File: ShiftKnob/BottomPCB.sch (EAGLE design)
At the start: 36 parts, among them IC2 UA78M05DCY, J1 AVR_SPI_PRG_6PTH, Q1 16MHz, Q2 MOSFET-NCHANNELSMD, Q3 MOSFET-PCHANNELSMD, Q4 MOSFET-NCHANNELSMD, Q5 MOSFET-NCHANNELSMD, Q6 MOSFET-NCHANNELSMD, U1 ATMEGA328, U3 FT232RL-BASICSSOP

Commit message: add 0.1" holes in bottom PCB.
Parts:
- added JP2, JP5: (no value), SparkFun-Connectors:M03PTH
- added U$2: 7-SEGMENT-DISPLAY-1"-RED, SparkFun-Displays:7-SEGMENT-DISPLAY-1"-RED
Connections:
- new net N$20: JP2.2
- new net N$26: JP2.1
- new net N$27: JP5.3
- new net N$28: JP5.2
- new net N$29: JP5.1
- new net N$3: JP2.3
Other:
- moved on the sheet: JP1
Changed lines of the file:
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@@
 <setting verticaltext="up"/>
 </settings>
-<grid distance="0.05" unitdist="inch" unit="inch" style="lines" multiple="1" display="no" altdistance="0.01" altunitdist="inch" altunit="inch"/>
+<grid distance="0.1" unitdist="inch" unit="inch" style="lines" multiple="1" display="no" altdistance="0.01" altunitdist="inch" altunit="inch"/>
 <layers>
 <layer number="1" name="Top" color="4" fill="1" visible="no" active="no"/>
@@
 <part name="P+5" library="SparkFun" deviceset="3.3V" device="" value="VCC"/>
 <part name="BUTTON" library="FORD_frames" deviceset="BUTTON_RIGHTANGLE_SMD" device=""/>
+<part name="U$2" library="SparkFun-Displays" deviceset="7-SEGMENT-DISPLAY-1&quot;-RED" device=""/>
+<part name="JP2" library="SparkFun-Connectors" deviceset="M03" device="PTH"/>
+<part name="JP5" library="SparkFun-Connectors" deviceset="M03" device="PTH"/>
 </parts>
 <sheets>
@@
 <instance part="FRAME1" gate="G$1" x="0" y="0"/>
 <instance part="FRAME1" gate="G$2" x="168.91" y="0"/>
-<instance part="JP1" gate="G$1" x="13.97" y="175.26"/>
+<instance part="JP1" gate="G$1" x="-34.29" y="177.8"/>
 <instance part="R2" gate="G$1" x="27.94" y="135.89" rot="R90"/>
 <instance part="GND3" gate="1" x="138.43" y="99.06"/>
@@
 <attribute name="NAME" x="132.08" y="110.49" size="1.778" layer="95" rot="R90"/>
 </instance>
+<instance part="U$2" gate="G$1" x="344.17" y="176.53"/>
+<instance part="JP2" gate="G$1" x="10.16" y="182.88"/>
+<instance part="JP5" gate="G$1" x="10.16" y="165.1"/>
 </instances>
 <busses>
@@
 <segment>
 <pinref part="JP1" gate="G$1" pin="1"/>
-<wire x1="19.05" y1="170.18" x2="29.21" y2="170.18" width="0.1524" layer="91"/>
-<label x="24.13" y="170.18" size="1.778" layer="95"/>
+<wire x1="-29.21" y1="172.72" x2="-19.05" y2="172.72" width="0.1524" layer="91"/>
+<label x="-24.13" y="172.72" size="1.778" layer="95"/>
 </segment>
 <segment>
@@
 <segment>
 <pinref part="JP1" gate="G$1" pin="2"/>
-<wire x1="19.05" y1="172.72" x2="29.21" y2="172.72" width="0.1524" layer="91"/>
-<label x="24.13" y="172.72" size="1.778" layer="95"/>
+<wire x1="-29.21" y1="175.26" x2="-19.05" y2="175.26" width="0.1524" layer="91"/>
+<label x="-24.13" y="175.26" size="1.778" layer="95"/>
 </segment>
 <segment>
@@
 <segment>
 <pinref part="JP1" gate="G$1" pin="3"/>
-<wire x1="19.05" y1="175.26" x2="29.21" y2="175.26" width="0.1524" layer="91"/>
-<label x="24.13" y="175.26" size="1.778" layer="95"/>
+<wire x1="-29.21" y1="177.8" x2="-19.05" y2="177.8" width="0.1524" layer="91"/>
+<label x="-24.13" y="177.8" size="1.778" layer="95"/>
 </segment>
 <segment>
@@
 <segment>
 <pinref part="JP1" gate="G$1" pin="4"/>
-<wire x1="19.05" y1="177.8" x2="29.21" y2="177.8" width="0.1524" layer="91"/>
-<label x="24.13" y="177.8" size="1.778" layer="95"/>
+<wire x1="-29.21" y1="180.34" x2="-19.05" y2="180.34" width="0.1524" layer="91"/>
+<label x="-24.13" y="180.34" size="1.778" layer="95"/>
 </segment>
 </net>
@@
 <segment>
 <pinref part="JP1" gate="G$1" pin="6"/>
-<wire x1="19.05" y1="182.88" x2="29.21" y2="182.88" width="0.1524" layer="91"/>
-<label x="24.13" y="182.88" size="1.778" layer="95"/>
+<wire x1="-29.21" y1="185.42" x2="-19.05" y2="185.42" width="0.1524" layer="91"/>
+<label x="-24.13" y="185.42" size="1.778" layer="95"/>
 </segment>
 </net>
@@
 <segment>
 <pinref part="JP1" gate="G$1" pin="5"/>
-<wire x1="19.05" y1="180.34" x2="29.21" y2="180.34" width="0.1524" layer="91"/>
-<label x="24.13" y="180.34" size="1.778" layer="95"/>
+<wire x1="-29.21" y1="182.88" x2="-19.05" y2="182.88" width="0.1524" layer="91"/>
+<label x="-24.13" y="182.88" size="1.778" layer="95"/>
 </segment>
 </net>
@@
 </segment>
 </net>
+<net name="N$3" class="0">
+<segment>
+<pinref part="JP2" gate="G$1" pin="3"/>
+<wire x1="17.78" y1="185.42" x2="25.4" y2="185.42" width="0.1524" layer="91"/>
+</segment>
+</net>
+<net name="N$20" class="0">
+<segment>
+<pinref part="JP2" gate="G$1" pin="2"/>
+<wire x1="17.78" y1="182.88" x2="25.4" y2="182.88" width="0.1524" layer="91"/>
+</segment>
+</net>
+<net name="N$26" class="0">
+<segment>
+<pinref part="JP2" gate="G$1" pin="1"/>
+<wire x1="17.78" y1="180.34" x2="25.4" y2="180.34" width="0.1524" layer="91"/>
+</segment>
+</net>
+<net name="N$27" class="0">
+<segment>
+<pinref part="JP5" gate="G$1" pin="3"/>
+<wire x1="17.78" y1="167.64" x2="25.4" y2="167.64" width="0.1524" layer="91"/>
+</segment>
+</net>
+<net name="N$28" class="0">
+<segment>
+<pinref part="JP5" gate="G$1" pin="2"/>
+<wire x1="17.78" y1="165.1" x2="25.4" y2="165.1" width="0.1524" layer="91"/>
+</segment>
+</net>
+<net name="N$29" class="0">
+<segment>
+<pinref part="JP5" gate="G$1" pin="1"/>
+<wire x1="17.78" y1="162.56" x2="25.4" y2="162.56" width="0.1524" layer="91"/>
+</segment>
+</net>

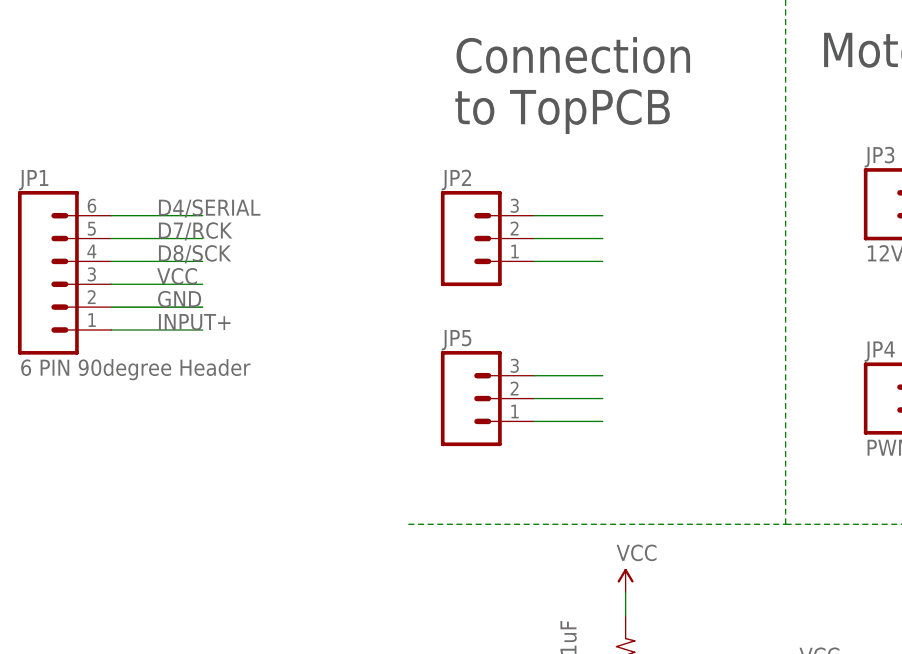
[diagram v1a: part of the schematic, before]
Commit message: remove 6 pin header. add (2) 4 pin headers and place in the correct location to match TopPCB.
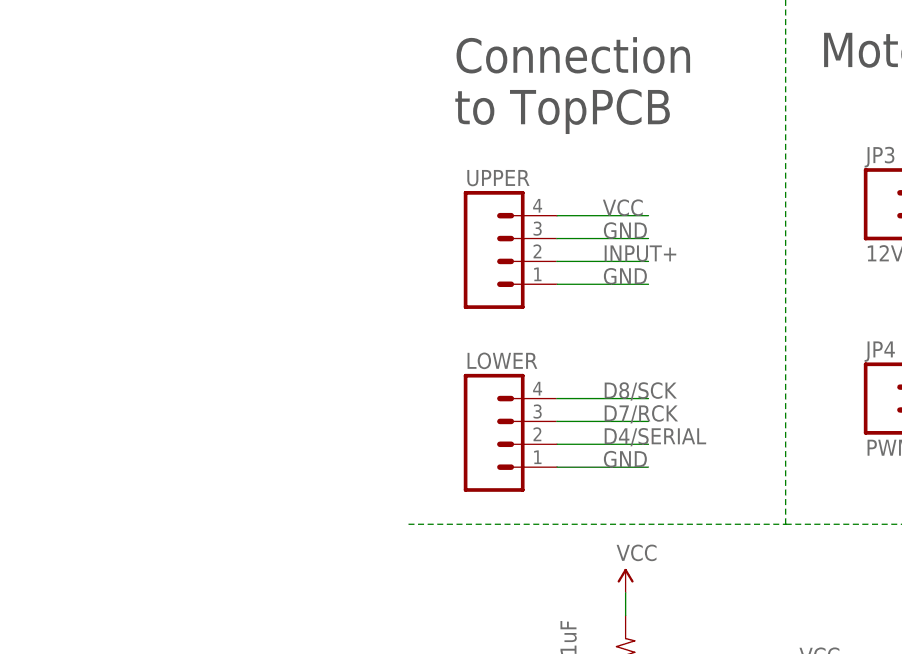
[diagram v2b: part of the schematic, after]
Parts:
- removed JP1: 6 PIN 90degree Header, SparkFun-Connectors:M06SIP
- removed JP2, JP5: (no value), SparkFun-Connectors:M03PTH
- added LOWER, UPPER: (no value), SparkFun-Connectors:M04PTH
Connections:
- removed net N$20: JP2.2
- removed net N$26: JP2.1
- removed net N$27: JP5.3
- removed net N$28: JP5.2
- removed net N$29: JP5.1
- removed net N$3: JP2.3
- net D4/SERIAL: now also LOWER.2; no longer JP1.6
- net D7/RCK: now also LOWER.3; no longer JP1.5
- net D8/SCK: now also LOWER.4; no longer JP1.4
- net GND: now also LOWER.1, UPPER.1, UPPER.3; no longer JP1.2
- net INPUT+: now also UPPER.2; no longer JP1.1
- net VCC: now also UPPER.4; no longer JP1.3
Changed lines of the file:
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@@
 <parts>
 <part name="FRAME1" library="FORD_frames" deviceset="FRAME_A_L" device=""/>
-<part name="JP1" library="SparkFun-Connectors" deviceset="M06" device="SIP" value="6 PIN 90degree Header"/>
 <part name="R2" library="SparkFun" deviceset="RESISTOR" device="0402-RES" value="10K"/>
 <part name="GND3" library="SparkFun" deviceset="GND" device=""/>
@@
 <part name="BUTTON" library="FORD_frames" deviceset="BUTTON_RIGHTANGLE_SMD" device=""/>
 <part name="U$2" library="SparkFun-Displays" deviceset="7-SEGMENT-DISPLAY-1&quot;-RED" device=""/>
-<part name="JP2" library="SparkFun-Connectors" deviceset="M03" device="PTH"/>
-<part name="JP5" library="SparkFun-Connectors" deviceset="M03" device="PTH"/>
+<part name="UPPER" library="SparkFun-Connectors" deviceset="M04" device="PTH"/>
+<part name="LOWER" library="SparkFun-Connectors" deviceset="M04" device="PTH"/>
 </parts>
 <sheets>
@@
 <instance part="FRAME1" gate="G$1" x="0" y="0"/>
 <instance part="FRAME1" gate="G$2" x="168.91" y="0"/>
-<instance part="JP1" gate="G$1" x="-34.29" y="177.8"/>
 <instance part="R2" gate="G$1" x="27.94" y="135.89" rot="R90"/>
 <instance part="GND3" gate="1" x="138.43" y="99.06"/>
@@
 </instance>
 <instance part="U$2" gate="G$1" x="344.17" y="176.53"/>
-<instance part="JP2" gate="G$1" x="10.16" y="182.88"/>
-<instance part="JP5" gate="G$1" x="10.16" y="165.1"/>
+<instance part="UPPER" gate="G$1" x="15.24" y="180.34"/>
+<instance part="LOWER" gate="G$1" x="15.24" y="160.02"/>
 </instances>
 <busses>
@@
 <net name="INPUT+" class="0">
 <segment>
-<pinref part="JP1" gate="G$1" pin="1"/>
-<wire x1="-29.21" y1="172.72" x2="-19.05" y2="172.72" width="0.1524" layer="91"/>
-<label x="-24.13" y="172.72" size="1.778" layer="95"/>
-</segment>
-<segment>
 <pinref part="Q3" gate="G$1" pin="D"/>
 <wire x1="167.64" y1="107.95" x2="167.64" y2="110.49" width="0.1524" layer="91"/>
@@
 <label x="170.18" y="110.49" size="1.778" layer="95"/>
 </segment>
+<segment>
+<pinref part="UPPER" gate="G$1" pin="2"/>
+<wire x1="20.32" y1="180.34" x2="30.48" y2="180.34" width="0.1524" layer="91"/>
+<label x="25.4" y="180.34" size="1.778" layer="95"/>
+</segment>
 </net>
 <net name="GND" class="0">
-<segment>
-<pinref part="JP1" gate="G$1" pin="2"/>
-<wire x1="-29.21" y1="175.26" x2="-19.05" y2="175.26" width="0.1524" layer="91"/>
-<label x="-24.13" y="175.26" size="1.778" layer="95"/>
-</segment>
 <segment>
 <wire x1="138.43" y1="107.95" x2="138.43" y2="101.6" width="0.1524" layer="91"/>
@@
 <pinref part="GND16" gate="1" pin="GND"/>
 </segment>
+<segment>
+<pinref part="UPPER" gate="G$1" pin="3"/>
+<wire x1="20.32" y1="182.88" x2="30.48" y2="182.88" width="0.1524" layer="91"/>
+<label x="25.4" y="182.88" size="1.778" layer="95"/>
+</segment>
+<segment>
+<pinref part="UPPER" gate="G$1" pin="1"/>
+<wire x1="20.32" y1="177.8" x2="30.48" y2="177.8" width="0.1524" layer="91"/>
+<label x="25.4" y="177.8" size="1.778" layer="95"/>
+</segment>
+<segment>
+<pinref part="LOWER" gate="G$1" pin="1"/>
+<wire x1="20.32" y1="157.48" x2="30.48" y2="157.48" width="0.1524" layer="91"/>
+<label x="25.4" y="157.48" size="1.778" layer="95"/>
+</segment>
 </net>
 <net name="VCC" class="0">
-<segment>
-<pinref part="JP1" gate="G$1" pin="3"/>
-<wire x1="-29.21" y1="177.8" x2="-19.05" y2="177.8" width="0.1524" layer="91"/>
-<label x="-24.13" y="177.8" size="1.778" layer="95"/>
-</segment>
 <segment>
 <wire x1="27.94" y1="143.51" x2="27.94" y2="140.97" width="0.1524" layer="91"/>
@@
 <wire x1="135.89" y1="54.61" x2="135.89" y2="58.42" width="0.1524" layer="91"/>
 <pinref part="P+2" gate="G$1" pin="3.3V"/>
+</segment>
+<segment>
+<pinref part="UPPER" gate="G$1" pin="4"/>
+<wire x1="20.32" y1="185.42" x2="30.48" y2="185.42" width="0.1524" layer="91"/>
+<label x="25.4" y="185.42" size="1.778" layer="95"/>
 </segment>
 </net>
@@
 </segment>
 <segment>
-<pinref part="JP1" gate="G$1" pin="4"/>
-<wire x1="-29.21" y1="180.34" x2="-19.05" y2="180.34" width="0.1524" layer="91"/>
-<label x="-24.13" y="180.34" size="1.778" layer="95"/>
+<pinref part="LOWER" gate="G$1" pin="4"/>
+<wire x1="20.32" y1="165.1" x2="30.48" y2="165.1" width="0.1524" layer="91"/>
+<label x="25.4" y="165.1" size="1.778" layer="95"/>
 </segment>
 </net>
@@
 </segment>
 <segment>
-<pinref part="JP1" gate="G$1" pin="6"/>
-<wire x1="-29.21" y1="185.42" x2="-19.05" y2="185.42" width="0.1524" layer="91"/>
-<label x="-24.13" y="185.42" size="1.778" layer="95"/>
+<pinref part="LOWER" gate="G$1" pin="2"/>
+<wire x1="20.32" y1="160.02" x2="30.48" y2="160.02" width="0.1524" layer="91"/>
+<label x="25.4" y="160.02" size="1.778" layer="95"/>
 </segment>
 </net>
@@
 </segment>
 <segment>
-<pinref part="JP1" gate="G$1" pin="5"/>
-<wire x1="-29.21" y1="182.88" x2="-19.05" y2="182.88" width="0.1524" layer="91"/>
-<label x="-24.13" y="182.88" size="1.778" layer="95"/>
+<pinref part="LOWER" gate="G$1" pin="3"/>
+<wire x1="20.32" y1="162.56" x2="30.48" y2="162.56" width="0.1524" layer="91"/>
+<label x="25.4" y="162.56" size="1.778" layer="95"/>
 </segment>
 </net>
@@
 </segment>
 </net>
-<net name="N$3" class="0">
-<segment>
-<pinref part="JP2" gate="G$1" pin="3"/>
-<wire x1="17.78" y1="185.42" x2="25.4" y2="185.42" width="0.1524" layer="91"/>
-</segment>
-</net>
-<net name="N$20" class="0">
-<segment>
-<pinref part="JP2" gate="G$1" pin="2"/>
-<wire x1="17.78" y1="182.88" x2="25.4" y2="182.88" width="0.1524" layer="91"/>
-</segment>
-</net>
-<net name="N$26" class="0">
-<segment>
-<pinref part="JP2" gate="G$1" pin="1"/>
-<wire x1="17.78" y1="180.34" x2="25.4" y2="180.34" width="0.1524" layer="91"/>
-</segment>
-</net>
-<net name="N$27" class="0">
-<segment>
-<pinref part="JP5" gate="G$1" pin="3"/>
-<wire x1="17.78" y1="167.64" x2="25.4" y2="167.64" width="0.1524" layer="91"/>
-</segment>
-</net>
-<net name="N$28" class="0">
-<segment>
-<pinref part="JP5" gate="G$1" pin="2"/>
-<wire x1="17.78" y1="165.1" x2="25.4" y2="165.1" width="0.1524" layer="91"/>
-</segment>
-</net>
-<net name="N$29" class="0">
-<segment>
-<pinref part="JP5" gate="G$1" pin="1"/>
-<wire x1="17.78" y1="162.56" x2="25.4" y2="162.56" width="0.1524" layer="91"/>
-</segment>
-</net>
